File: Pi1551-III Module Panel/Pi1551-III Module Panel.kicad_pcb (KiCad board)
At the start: 2 copper layers, 100 x 23.2 mm, 15 parts, among them IC1 OLED, J1 Module Panel, M1 Mounting_Pin, M2 Mounting_Pin, M3 Mounting_Pin, M4 Mounting_Pin, SW1 BACK, SW2 INSERT

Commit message: upgrade to KiCad 9.0.7
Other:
- net class Default removed
- net class PWR removed
- board text added: "Pi1551-III Panel"
- board text removed: "BulkyMIDI-32 Pi1551-III Panel (rev. A) github.com/tebl"

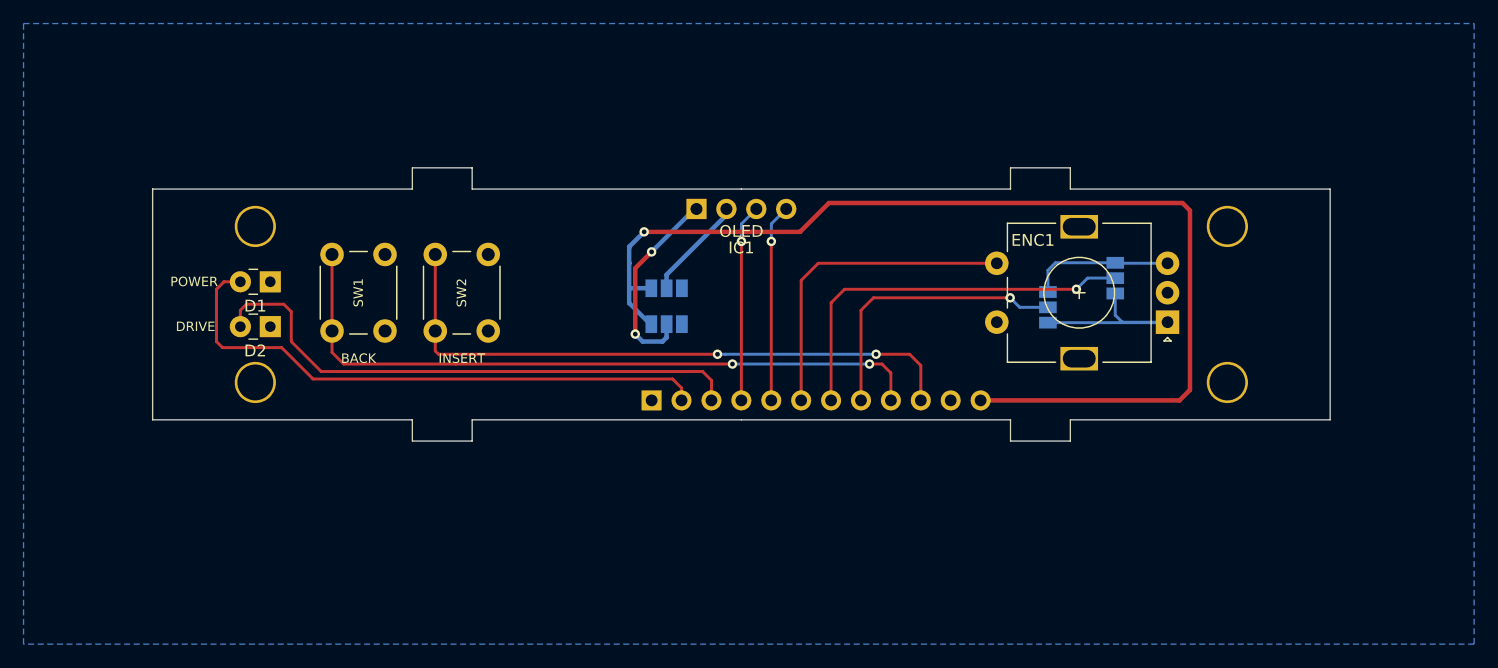
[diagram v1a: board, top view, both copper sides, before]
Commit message: PI1551 branding and Microgramma font labels
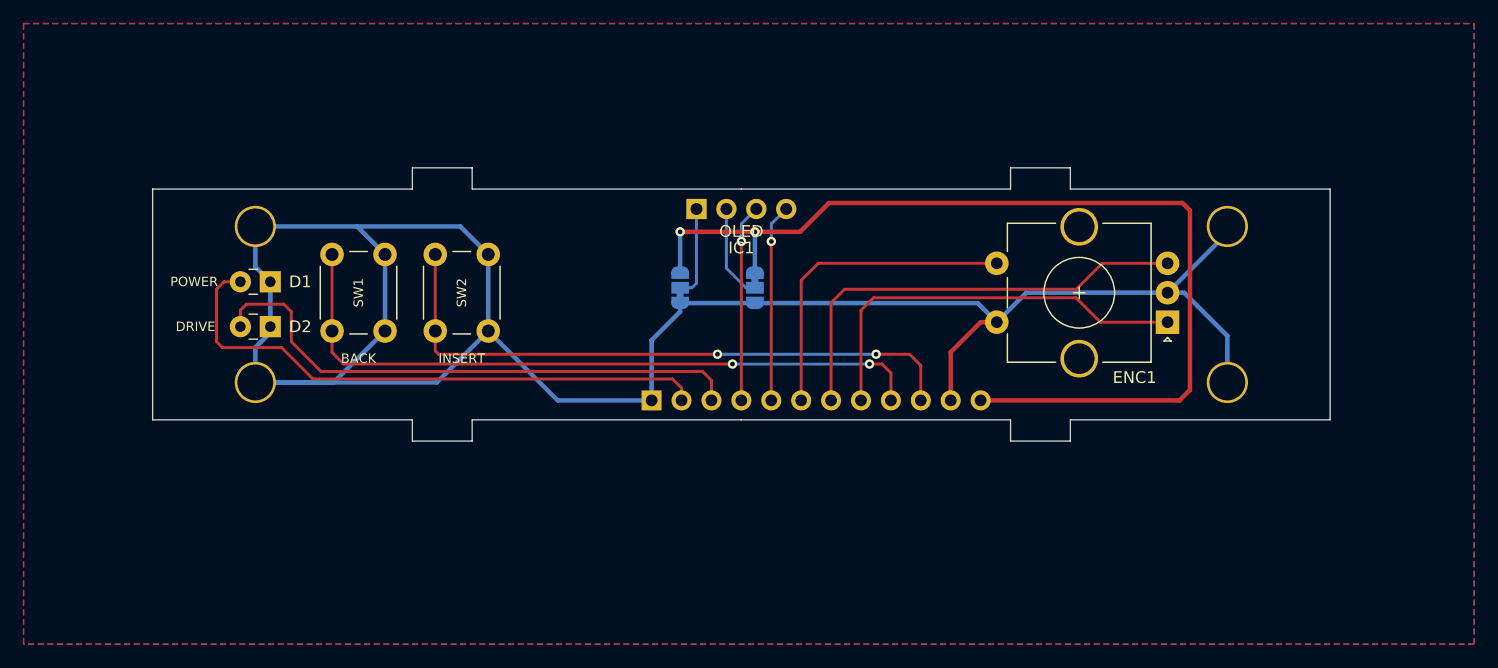
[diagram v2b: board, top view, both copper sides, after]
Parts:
- removed JP1: CLK, Jumper:SolderJumper-3_P1.3mm_Open_Pad1.0x1.5mm
- removed JP2: DAT, Jumper:SolderJumper-3_P1.3mm_Open_Pad1.0x1.5mm
- ENC1: value Rotary_Encoder_Switch -> RotaryEncoder_Switch; footprint Rotary_Encoder:RotaryEncoder_Alps_EC11E-Switch_Vertical_H20mm -> Rotary_Encoder:RotaryEncoder_Alps_EC11E-Switch_Vertical_H20mm_CircularMountingHoles
- JP3: value P1_GND -> SolderJumper_3_Bridged12; footprint Jumper:SolderJumper-3_P1.3mm_Open_Pad1.0x1.5mm -> Jumper:SolderJumper-3_P1.3mm_Bridged12_RoundedPad1.0x1.5mm_NumberLabels
- JP4: value P2_VCC -> SolderJumper_3_Bridged12; footprint Jumper:SolderJumper-3_P1.3mm_Open_Pad1.0x1.5mm -> Jumper:SolderJumper-3_P1.3mm_Bridged12_RoundedPad1.0x1.5mm_NumberLabels
- moved JP3 8.11 mm to (142.2, 121.2), turned to -90 degrees
- moved JP4 1.15 mm to (135.9, 121.2), turned to 90 degrees
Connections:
- ENC1 pad A: /A -> SW_DOWN
- ENC1 pad B: /B -> SW_UP
- IC1 pad 1: Net-(IC1-Pad1) -> Net-(IC1-GND)
- IC1 pad 2: Net-(IC1-Pad2) -> Net-(IC1-VCC)
- JP3 pad 1: GND -> VCC
- JP3 pad 2: Net-(IC1-Pad1) -> Net-(IC1-VCC)
- JP3 pad 3: VCC -> GND
- JP4 pad 1: VCC -> GND
- JP4 pad 2: Net-(IC1-Pad2) -> Net-(IC1-GND)
- JP4 pad 3: GND -> VCC
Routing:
- net GND: track 0.04 -> 181.9 mm
- net Net-(IC1-Pad1): track 17.1 -> 0.00 mm, vias 2 -> 0
- net /A: track 16.7 -> 0.00 mm
- net /B: track 12.3 -> 0.00 mm
- net SW_DOWN: track 24.3 -> 35.0 mm, vias 1 -> 0
- net Net-(IC1-Pad2): track 8.84 -> 0.00 mm
- net Net-(IC1-VCC): track 0.00 -> 8.65 mm
- net Net-(IC1-GND): track 0.00 -> 8.02 mm
- net VCC: track 92.7 -> 84.9 mm, vias 1 -> 2
- net SW_UP: track 33.3 -> 38.3 mm, vias 1 -> 0
- added copper zone on F.Cu, net GND
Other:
- board text added: "SDA|SCL|(PIN2)|(PIN1)"
- board text added: "VCC|PIN1|GND"
- board text added: "VCC|PIN2|GND"

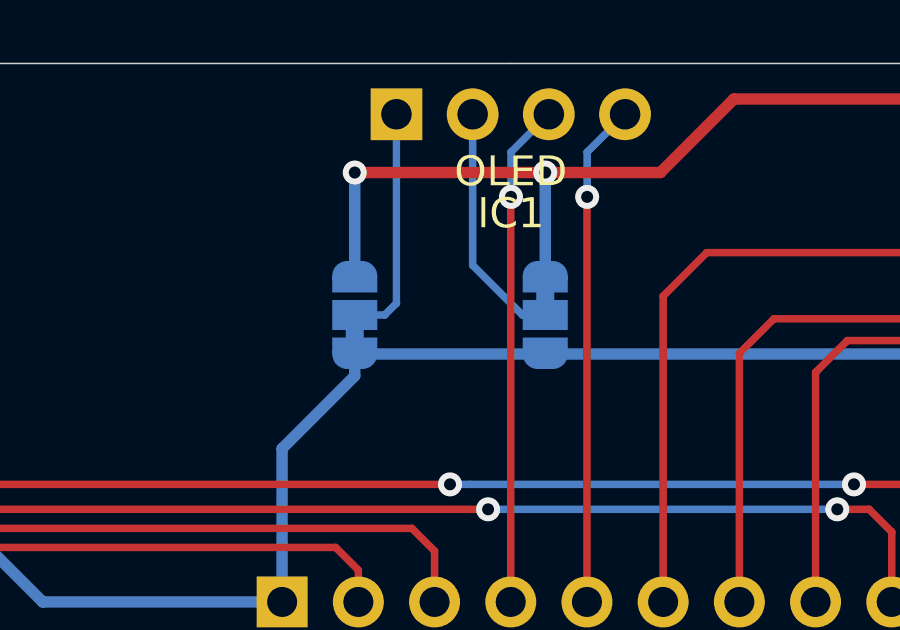
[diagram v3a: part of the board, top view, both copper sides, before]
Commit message: change jumpers to be open - it's too difficult to cut them once panel is soldered in
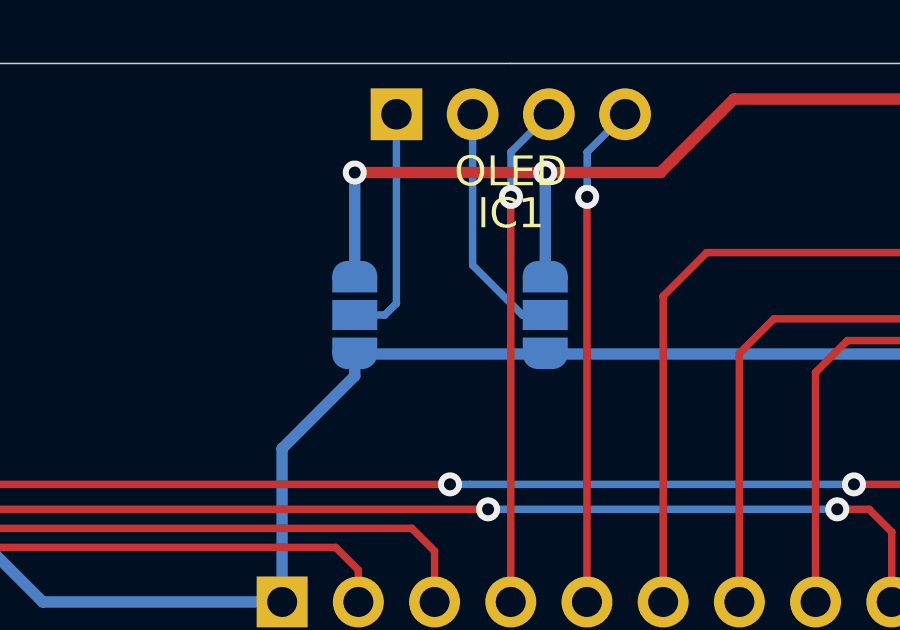
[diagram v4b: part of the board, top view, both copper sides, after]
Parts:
- JP3, JP4: value SolderJumper_3_Bridged12 -> SolderJumper_3_Open; footprint Jumper:SolderJumper-3_P1.3mm_Bridged12_RoundedPad1.0x1.5mm_NumberLabels -> Jumper:SolderJumper-3_P1.3mm_Open_RoundedPad1.0x1.5mm_NumberLabels
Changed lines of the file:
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@@
 	(title_block
 		(title "Pi1551-III Module (Panel)")
-		(date "2026-02-02")
-		(rev "1")
+		(date "2026-03-03")
+		(rev "2")
 	)
 	(layers
@@
 	)
 	(setup
+		(stackup
+			(layer "F.SilkS"
+				(type "Top Silk Screen")
+			)
+			(layer "F.Paste"
+				(type "Top Solder Paste")
+			)
+			(layer "F.Mask"
+				(type "Top Solder Mask")
+				(thickness 0.01)
+			)
+			(layer "F.Cu"
+				(type "copper")
+				(thickness 0.035)
+			)
+			(layer "dielectric 1"
+				(type "core")
+				(thickness 1.51)
+				(material "FR4")
+				(epsilon_r 4.5)
+				(loss_tangent 0.02)
+			)
+			(layer "B.Cu"
+				(type "copper")
+				(thickness 0.035)
+			)
+			(layer "B.Mask"
+				(type "Bottom Solder Mask")
+				(thickness 0.01)
+			)
+			(layer "B.Paste"
+				(type "Bottom Solder Paste")
+			)
+			(layer "B.SilkS"
+				(type "Bottom Silk Screen")
+			)
+			(copper_finish "None")
+			(dielectric_constraints no)
+		)
 		(pad_to_mask_clearance 0)
 		(allow_soldermask_bridges_in_footprints no)
@@
 		(sheetname "/")
 		(sheetfile "Pi1551-III Module Panel.kicad_sch")
-		(attr through_hole)
+		(attr through_hole exclude_from_bom)
 		(fp_circle
 			(center 0 0)
@@
 		(sheetname "/")
 		(sheetfile "Pi1551-III Module Panel.kicad_sch")
-		(attr through_hole)
+		(attr through_hole exclude_from_bom)
 		(fp_circle
 			(center 0 0)
@@
 		(sheetname "/")
 		(sheetfile "Pi1551-III Module Panel.kicad_sch")
-		(attr through_hole)
+		(attr through_hole exclude_from_bom)
 		(fp_circle
 			(center 0 0)
@@
 		(sheetname "/")
 		(sheetfile "Pi1551-III Module Panel.kicad_sch")
-		(attr through_hole)
+		(attr through_hole exclude_from_bom)
 		(fp_circle
 			(center 0 0)
@@
 		)
 	)
-	(footprint "Jumper:SolderJumper-3_P1.3mm_Bridged12_RoundedPad1.0x1.5mm_NumberLabels"
+	(footprint "Jumper:SolderJumper-3_P1.3mm_Open_RoundedPad1.0x1.5mm_NumberLabels"
 		(layer "B.Cu")
 		(at 142.24 121.158 -90)
-		(descr "SMD Solder 3-pad Jumper, 1x1.5mm rounded Pads, 0.3mm gap, pads 1-2 bridged with 1 copper strip, labeled with numbers")
-		(tags "net tie solder jumper bridged")
+		(descr "SMD Solder 3-pad Jumper, 1x1.5mm rounded Pads, 0.3mm gap, open, labeled with numbers")
+		(tags "solder jumper open")
 		(property "Reference" "JP3"
 			(at 0 1.8 90)
@@
 			)
 		)
-		(property "Value" "SolderJumper_3_Bridged12"
+		(property "Value" "SolderJumper_3_Open"
 			(at 0 -1.9 90)
 			(layer "B.Fab")
@@
 			)
 		)
-		(property "Description" "3-pole Solder Jumper, pins 1+2 closed/bridged"
+		(property "Description" "Solder Jumper, 3-pole, open"
 			(at 0 0 90)
 			(unlocked yes)
@@
 			)
 		)
-		(property ki_fp_filters "SolderJumper*Bridged12*")
+		(property ki_fp_filters "SolderJumper*Open*")
 		(sheetname "/")
 		(sheetfile "Pi1551-III Module Panel.kicad_sch")
 		(zone_connect 1)
 		(attr exclude_from_pos_files exclude_from_bom allow_soldermask_bridges)
-		(net_tie_pad_groups "1, 2")
-		(fp_poly
-			(pts
-				(xy -0.9 0.3) (xy -0.4 0.3) (xy -0.4 -0.3) (xy -0.9 -0.3)
-			)
-			(stroke
-				(width 0)
-				(type solid)
-			)
-			(fill yes)
-			(layer "B.Cu")
-		)
 		(fp_rect
 			(start -0.75 0.75)
@@
 			)
 			(primitives
-				(gr_poly
-					(pts
-						(xy 0.55 -0.75) (xy 0 -0.75) (xy 0 0.75) (xy 0.55 0.75)
-					)
-					(width 0)
-					(fill yes)
-				)
 				(gr_circle
 					(center 0 -0.25)
@@
 					(fill yes)
 				)
+				(gr_poly
+					(pts
+						(xy 0.55 -0.75) (xy 0 -0.75) (xy 0 0.75) (xy 0.55 0.75)
+					)
+					(width 0)
+					(fill yes)
+				)
 			)
 		)
@@
 		(embedded_fonts no)
 	)
-	(footprint "Jumper:SolderJumper-3_P1.3mm_Bridged12_RoundedPad1.0x1.5mm_NumberLabels"
+	(footprint "Jumper:SolderJumper-3_P1.3mm_Open_RoundedPad1.0x1.5mm_NumberLabels"
 		(layer "B.Cu")
 		(at 135.89 121.158 90)
-		(descr "SMD Solder 3-pad Jumper, 1x1.5mm rounded Pads, 0.3mm gap, pads 1-2 bridged with 1 copper strip, labeled with numbers")
-		(tags "net tie solder jumper bridged")
+		(descr "SMD Solder 3-pad Jumper, 1x1.5mm rounded Pads, 0.3mm gap, open, labeled with numbers")
+		(tags "solder jumper open")
 		(property "Reference" "JP4"
-			(at 0 1.8 90)
+			(at 0 1.8 270)
 			(layer "B.SilkS")
 			(effects
@@
 			)
 		)
-		(property "Value" "SolderJumper_3_Bridged12"
-			(at 0 -1.9 90)
+		(property "Value" "SolderJumper_3_Open"
+			(at 0 -1.9 270)
 			(layer "B.Fab")
 			(hide yes)
@@
 			)
 		)
-		(property "Description" "3-pole Solder Jumper, pins 1+2 closed/bridged"
+		(property "Description" "Solder Jumper, 3-pole, open"
 			(at 0 0 270)
 			(unlocked yes)
@@
 			)
 		)
-		(property ki_fp_filters "SolderJumper*Bridged12*")
+		(property ki_fp_filters "SolderJumper*Open*")
 		(sheetname "/")
 		(sheetfile "Pi1551-III Module Panel.kicad_sch")
 		(zone_connect 1)
 		(attr exclude_from_pos_files exclude_from_bom allow_soldermask_bridges)
-		(net_tie_pad_groups "1, 2")
-		(fp_poly
-			(pts
-				(xy -0.9 0.3) (xy -0.4 0.3) (xy -0.4 -0.3) (xy -0.9 -0.3)
-			)
-			(stroke
-				(width 0)
-				(type solid)
-			)
-			(fill yes)
-			(layer "B.Cu")
-		)
 		(fp_rect
 			(start -0.75 0.75)
@@
 		)
 		(fp_text user "3"
-			(at 2.6 0 90)
+			(at 2.6 0 270)
 			(layer "B.SilkS")
 			(effects
@@
 		)
 		(fp_text user "1"
-			(at -2.6 0 90)
+			(at -2.6 0 270)
 			(layer "B.SilkS")
 			(effects
@@
 			)
 			(primitives
-				(gr_poly
-					(pts
-						(xy 0.55 -0.75) (xy 0 -0.75) (xy 0 0.75) (xy 0.55 0.75)
-					)
-					(width 0)
-					(fill yes)
-				)
 				(gr_circle
 					(center 0 -0.25)
@@
 					(width 0)
 					(fill yes)
+				)
+				(gr_poly
+					(pts
+						(xy 0.55 -0.75) (xy 0 -0.75) (xy 0 0.75) (xy 0.55 0.75)
+					)
+					(width 0)
+					(fill yes)
